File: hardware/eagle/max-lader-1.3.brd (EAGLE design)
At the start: 97.7 x 68.2 mm, 72 parts, among them IC1 OPA343, IC2 LM385-2.5, IC3 ICL 7667, IC4 7805, IC5 MEGA168-P, Q1 IRF4905, Q2 16MHz, Q3 IRFZ 48N, Q4 IRFZ 48N

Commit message: eagle files
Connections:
- net N$1 renamed INPUT_GATE
- net N$10 renamed BOOST_GATE
- net N$15 renamed BOOST_CTRL
- net N$3 renamed BUCK_CTRL
- net N$4 renamed BUCK_GATE
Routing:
- net GND: track 651.0 -> 630.1 mm, vias 2 -> 4
- net L+3: track 54.2 -> 48.1 mm
- added copper zone on layer 1, net AKKU+
- added copper zone on layer 1, net I_SENS
- added copper zone on layer 16, net I_SENS
- added copper zone on layer 1, net L+2
- added copper zone on layer 16, net L+2
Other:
- board size 97.7 x 68.2 mm -> 97.6 x 68.2 mm
- board text added: "V1.4"
- board text removed: "V1.3"

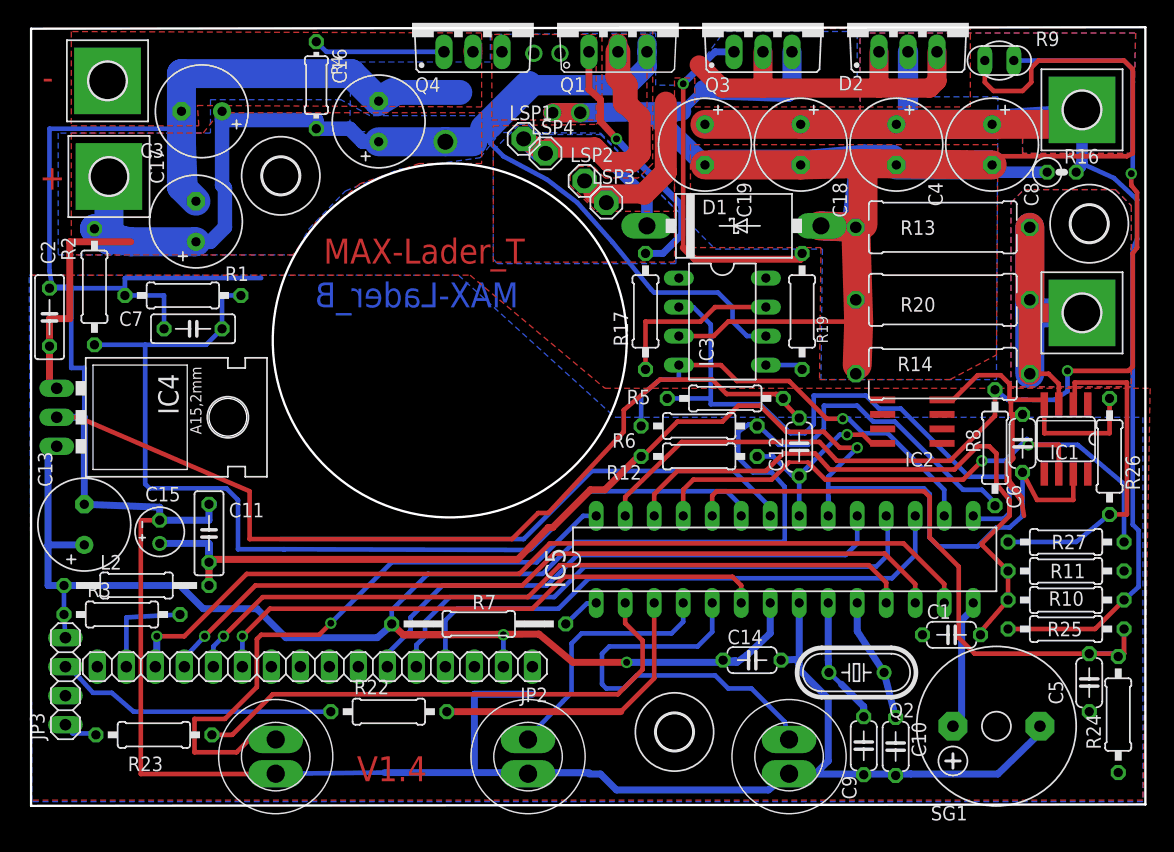
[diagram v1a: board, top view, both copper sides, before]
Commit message: layout version 1.5 with 1k protection resistors for icl7667 failure on overvoltage, it will kill the atmega168 without
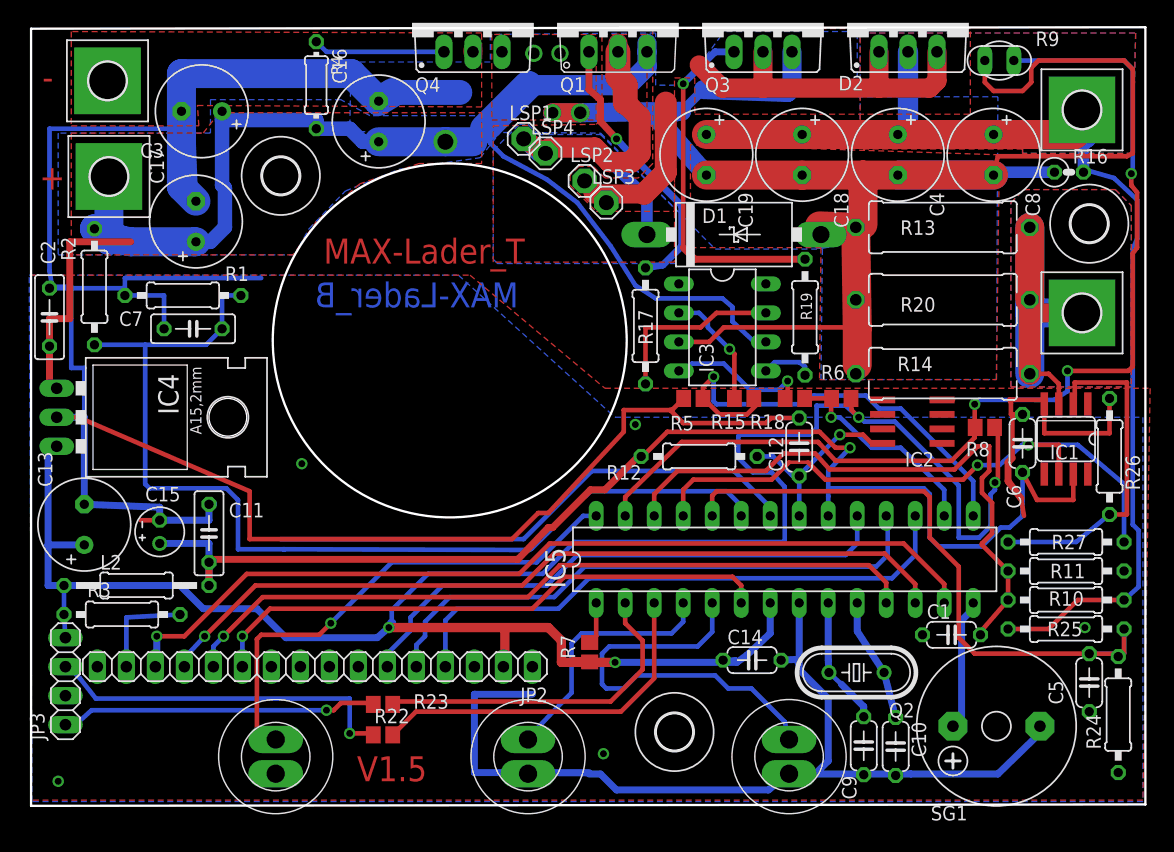
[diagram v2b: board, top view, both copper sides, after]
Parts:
- added R15, R18: 1k, rcl:R0805
- R22, R23, R5, R6, R8: device rcl:0207/10 -> rcl:R0805
- R7: device rcl:0207/15 -> rcl:R0805
- moved R23 20.2 mm to (32.8, 11.4)
- moved R6 12.7 mm to (72.9, 38.2)
- moved R7 10.0 mm to (50.9, 16.0), turned to 270 degrees
- moved R5 2.79 mm to (59.9, 38.2), turned to 0 degrees
- moved R22 2.09 mm to (32.8, 8.76)
- moved R8 1.99 mm to (85.5, 35.7), turned to 0 degrees
- moved R17 1.27 mm to (55.8, 44.6)
- moved C8 0.90 mm to (86.2, 59.6)
- moved C19 0.90 mm to (61.1, 59.6)
- moved C18 0.90 mm to (69.5, 59.6)
- moved C4 0.90 mm to (77.9, 59.6)
- moved D1 0.76 mm to (63.5, 52.6)
- moved R16 0.64 mm to (92.8, 58.0)
- moved R19 0.57 mm to (69.7, 45.3)
- moved IC3 0.51 mm to (62.5, 44.5)
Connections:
- new net N$1: IC3.4, R18.1
- new net N$3: IC3.2, R15.1
- net PWM_DOWN: now also R15.2; no longer IC3.2
- net PWM_UP: now also R18.2; no longer IC3.4
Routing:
- net GND: track 630.1 -> 546.2 mm, vias 4 -> 9
- net RXD_OUT: track 3.33 -> 27.8 mm, vias 0 -> 1
- net PWM_UP: track 37.8 -> 18.8 mm
- net RXD: track 46.6 -> 30.7 mm
- net PWM_DOWN: track 53.6 -> 40.1 mm, vias 0 -> 1
- net N$1: track 0.00 -> 12.8 mm, vias 0 -> 1
- net L: track 55.5 -> 44.5 mm
- net N$3: track 0.00 -> 10.5 mm, vias 0 -> 1
- net AKKU+: track 143.0 -> 135.2 mm
- net +5V: track 187.4 -> 194.2 mm, vias 2 -> 4
- net TXD_OUT: track 24.8 -> 31.3 mm, vias 0 -> 1
- net TXD: track 26.0 -> 31.6 mm
- net AVCC: track 119.5 -> 113.9 mm
- net BUCK_GATE: track 23.2 -> 24.2 mm
- net BOOST_CTRL: track 3.68 -> 4.63 mm
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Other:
- board text added: "V1.5"
- board text removed: "V1.4"
